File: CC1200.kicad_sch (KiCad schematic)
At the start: 55 parts, among them U3 CC1200, U4 MCP6001-OT, U8 MCP41010, X1 40MHz

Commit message: Revert "Stephen"
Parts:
- removed AE1: Antenna_Shield, Connector_Coaxial:SMA_BAT_Wireless_BWSMA-KWE-Z001, symbol Device:Antenna_Shield
- removed C14: DNM, Capacitor_SMD:C_0402_1005Metric, symbol Device:C
- removed C38, C39, C46: 0.1uF, Capacitor_SMD:C_0402_1005Metric, symbol Device:C
- removed C43, C44, C45: 100pF, Capacitor_SMD:C_0402_1005Metric, symbol Device:C
- removed C47: 10nF, Capacitor_SMD:C_0402_1005Metric, symbol Device:C
- removed JP1: SolderJumper_2_Open, Jumper:SolderJumper-2_P1.3mm_Open_RoundedPad1.0x1.5mm, symbol Jumper:SolderJumper_2_Open
- removed JP2: SolderJumper_2_Bridged, Jumper:SolderJumper-2_P1.3mm_Bridged_RoundedPad1.0x1.5mm, symbol Jumper:SolderJumper_2_Bridged
- removed L8: 22nH, Inductor_SMD:L_0402_1005Metric, symbol pspice:INDUCTOR
- removed R14: 1000, Resistor_SMD:R_0402_1005Metric, symbol Device:R_US
- removed R16: 1k, Resistor_SMD:R_0402_1005Metric, symbol Device:R_Small_US
- removed R2: 100, Resistor_SMD:R_0402_1005Metric, symbol Device:R_US
- removed RFAMP1: RA07H4047M-101, RA07H4047M:RA07H4047M101_HORIZ, symbol RA07H4047M-101:RA07H4047M-101
- removed RFSWITCH2: 4259-63, PE4259-63:SOT65P210X110-6N, symbol 4259-63:4259-63
- removed TH1: PT100, Resistor_SMD:R_0603_1608Metric, symbol Sensor_Temperature:PT100
- removed U4: MCP6001-OT, Package_TO_SOT_SMD:SOT-23-5, symbol Amplifier_Operational:MCP6001-OT
- removed U8: MCP41010, MCP41010:SOIC127P599X175-8N, symbol Potentiometer_Digital:MCP41010
- added A: AMP, symbol Device:R
- added RV1: R_Potentiometer, symbol Device:R_Potentiometer
- added SW1, SW2: SW_SPDT, symbol Switch:SW_SPDT
- C15, C17, C18, C19, C23, C24, C25, C28, C29: LCSC C272875 -> (none); LCSC Part (none) -> C508865
- C16: LCSC C16772 -> (none); LCSC Part (none) -> C16772
- C20, C22: LCSC C15195 -> (none); LCSC Part (none) -> C15195
- C21: value 1.5nF -> 1.8nF; LCSC C107022 -> (none); LCSC Part (none) -> C162192
- C26: LCSC C1572 -> (none); LCSC Part (none) -> C335543
- C27: LCSC C126492 -> (none); LCSC Part (none) -> C126492
- C30: LCSC C106223 -> (none); LCSC Part (none) -> C86288
- C31, C36: value 20pF -> 10pF; LCSC C1554 -> (none); LCSC Part (none) -> C32949
- C32, C33, C35: LCSC C60220 -> (none); LCSC Part (none) -> C281761
- C34: LCSC C325452 -> (none); LCSC Part (none) -> C159806
- C37: LCSC C41744 -> (none); LCSC Part (none) -> C325456
- L1, L2: footprint Inductor_SMD:L_0402_1005Metric -> Capacitor_SMD:C_0402_1005Metric; LCSC C167482 -> (none); LCSC Part (none) -> C167484
- L3: footprint Inductor_SMD:L_0402_1005Metric -> Capacitor_SMD:C_0402_1005Metric
- L4: footprint Inductor_SMD:L_0402_1005Metric -> Capacitor_SMD:C_0402_1005Metric; LCSC C12669 -> (none); LCSC Part (none) -> C12669
- L5, L6: footprint Inductor_SMD:L_0402_1005Metric -> Capacitor_SMD:C_0402_1005Metric; LCSC C94079 -> (none); LCSC Part (none) -> C27143
- L7: value 43nH -> 22nH; footprint Inductor_SMD:L_0402_1005Metric -> Capacitor_SMD:C_0402_1005Metric; LCSC C167478 -> (none); LCSC Part (none) -> C12670
- R13: footprint Resistor_SMD:R_0402_1005Metric -> Capacitor_SMD:C_0402_1005Metric; LCSC C138289 -> (none); LCSC Part (none) -> C138289
- R8: footprint Resistor_SMD:R_0402_1005Metric -> Capacitor_SMD:C_0402_1005Metric; LCSC C25796 -> (none); LCSC Part (none) -> C25796
- R9: value 18 -> 18k; footprint Resistor_SMD:R_0402_1005Metric -> Capacitor_SMD:C_0402_1005Metric; LCSC C2929991 -> (none); LCSC Part (none) -> C25084
- U3: LCSC C122881 -> (none); LCSC Part (none) -> C122881
- X1: LCSC C9010 -> (none); LCSC Part (none) -> C9010
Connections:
- net GND: now also C35.2
- net RX: no longer C33.1, L3.2
- net at L7.1: now also C34.1, C35.1, L5.2; no longer C37.1
- net at R13.1: now also C37.1, L7.2
- new net: A.1, SW1.1 (A)
- new net: SW1.3 (C), SW2.3 (C)
- new net: A.2, SW2.1 (A)
- new net: C33.1, L3.2, L6.1
- new net ANT: SW2.2 (B)
- new net CC1200: SW1.2 (B)
- now unconnected: U3.18 (TRX_SW)
- no-connect marks 1 -> 2
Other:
- note added: "TODO: Verify TX vs RX topology + matching Switch from seperate TX/RX to OG coupled RX / TX (do a bit of research first to which is better) Add amp bypass switch Add amp Add DPOT + OPAMP Buffer for Gate Voltage Add RTD (temp sensor)"
- note removed: "* Data sheet uses 1k pull-ups, can change back to 10k if needed."
- note removed: "*In single-pin control configuration, since we want no amplification by default, CTRL pin 4 is pulled high by default, allowing signal path of RFC -> RF1"
- note removed: "*RTD100 0603 is low on stock (~250), may need to replace with something else if it goes out of stock, such as a more complicated sensor or ic. Also may want to swap VD orientation."
- note removed: "1.8 nF -> 1.5 nF (changed from RS)"
- note removed: "Changed C31 and C36 to 20 pF from 10 pF each based on C9010 crystal needing 15 pF load capacitance overall, and using equation C1=C2=2*(C_L-C_stray), approximating C_stray as 5 pF."
- note removed: "TEMPERATURE SENSING"
- note removed: "keep dpot and op amp close to stm32, far from antenna"
- moved on the sheet: C37, L4, L5, L6, L7, R13

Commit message: checked matching network on CC1200 schematic
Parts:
- added C14: DNM, Capacitor_SMD:C_0402_1005Metric, symbol Device:C
- added L8: 22nH, Inductor_SMD:L_0402_1005Metric, symbol pspice:INDUCTOR
- C15, C17, C18, C19, C23, C24, C25, C28, C29: LCSC (none) -> C272875; LCSC Part C508865 -> (none)
- C16: LCSC (none) -> C16772; LCSC Part C16772 -> (none)
- C20, C22: LCSC (none) -> C15195; LCSC Part C15195 -> (none)
- C21: value 1.8nF -> 1.5nF; LCSC (none) -> C107022; LCSC Part C162192 -> (none)
- C26: LCSC (none) -> C1572; LCSC Part C335543 -> (none)
- C27: LCSC (none) -> C126492; LCSC Part C126492 -> (none)
- C30: LCSC (none) -> C106223; LCSC Part C86288 -> (none)
- C31, C36: value 10pF -> 20pF; LCSC (none) -> C1554; LCSC Part C32949 -> (none)
- C32, C33, C35: LCSC (none) -> C60220; LCSC Part C281761 -> (none)
- C34: LCSC (none) -> C325452; LCSC Part C159806 -> (none)
- C37: LCSC (none) -> C41744; LCSC Part C325456 -> (none)
- L1, L2: footprint Capacitor_SMD:C_0402_1005Metric -> Inductor_SMD:L_0402_1005Metric; LCSC (none) -> C167482; LCSC Part C167484 -> (none)
- L3: footprint Capacitor_SMD:C_0402_1005Metric -> Inductor_SMD:L_0402_1005Metric
- L4: footprint Capacitor_SMD:C_0402_1005Metric -> Inductor_SMD:L_0402_1005Metric; LCSC (none) -> C12669; LCSC Part C12669 -> (none)
- L5, L6: footprint Capacitor_SMD:C_0402_1005Metric -> Inductor_SMD:L_0402_1005Metric; LCSC (none) -> C94079; LCSC Part C27143 -> (none)
- L7: value 22nH -> 43nH; footprint Capacitor_SMD:C_0402_1005Metric -> Inductor_SMD:L_0402_1005Metric; LCSC (none) -> C167478; LCSC Part C12670 -> (none)
- R8: footprint Capacitor_SMD:C_0402_1005Metric -> Resistor_SMD:R_0402_1005Metric; LCSC (none) -> C25796; LCSC Part C25796 -> (none)
- R9: value 18k -> 18; footprint Capacitor_SMD:C_0402_1005Metric -> Resistor_SMD:R_0402_1005Metric; LCSC (none) -> C2929991; LCSC Part C25084 -> (none)
- X1: LCSC (none) -> C9010; LCSC Part C9010 -> (none)
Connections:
- net at C37.1, L7.2: now also C14.1, L8.1; no longer R13.1
- new net: C14.2, L8.2, R13.1
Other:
- note added: "*Check with Ethan that we are not using external oscillator, if so this should be fine just tied to ground, but reference schematic looks different."
- note added: "*Don't know if this capacitor should connect here, depends on if we are using TRX_SW pin on CC1200 and if we are or aren't coupling the LNA and PA pins."
- note added: "1.8 nF -> 1.5 nF (changed from RS)"
- note added: "Changed C31 and C36 to 20 pF from 10 pF each based on C9010 crystal needing 15 pF load capacitance overall, and using equation C1=C2=2*(C_L-C_stray), approximating C_stray as 5 pF."
- note added: "TODO: Verify TX vs RX topology + matching (DONE) Switch from seperate TX/RX to OG coupled RX / TX (do a bit of research first to which is better) Add amp bypass switch Add amp Add DPOT + OPAMP Buffer for Gate Voltage Add RTD (temp sensor)"
- note removed: "TODO: Verify TX vs RX topology + matching Switch from seperate TX/RX to OG coupled RX / TX (do a bit of research first to which is better) Add amp bypass switch Add amp Add DPOT + OPAMP Buffer for Gate Voltage Add RTD (temp sensor)"
- moved on the sheet: C37, L6, R13

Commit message: completed most of radio schematic
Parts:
- removed A: AMP, symbol Device:R
- removed RV1: R_Potentiometer, symbol Device:R_Potentiometer
- removed SW1, SW2: SW_SPDT, symbol Switch:SW_SPDT
- added C38, C39, C40: 100pF, Capacitor_SMD:C_0402_1005Metric, symbol Device:C
- added C41, C42: 33pF, Capacitor_SMD:C_0402_1005Metric, symbol Device:C
- added J6: SMA_CONNECTOR, Connector_Coaxial:SMA_Amphenol_901-143_Horizontal, symbol SMA_CONNECTOR:SMA_CONNECTOR
- added R14, R2: 4.7k, Resistor_SMD:R_0402_1005Metric, symbol Device:R_Small_US
- added RFAMP: ~, symbol RA07H4047M:RA07H4047M_RF_MOSFET_AMPLIFIER
- added RFSWITCH: SKY13351-378LF, SKY13351-378LF:QFN6-LF, symbol SKY13351-378LF:SKY13351-378LF
- added TH1: Thermistor_US, symbol Device:Thermistor_US
- added U4: MCP6001-OT, Package_TO_SOT_SMD:SOT-23-5, symbol Amplifier_Operational:MCP6001-OT
- R13: footprint Capacitor_SMD:C_0402_1005Metric -> Resistor_SMD:R_0402_1005Metric; LCSC (none) -> C138289; LCSC Part C138289 -> (none)
- U3: LCSC (none) -> C122881; LCSC Part C122881 -> (none)
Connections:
- net +3.3V: now also R2.2
- net GND: now also C41.2, C42.1, J6.G1, J6.G2, J6.G3, J6.G4, R14.1, RFAMP.5 (GND), RFSWITCH.2; no longer C35.2
- net RX: now also C33.1, L3.2
- net TX: now also C38.1
- net at U3.18 (TRX_SW): now also C35.1, L6.1
- net at C34.1, L5.2, L7.1: now also C35.2; no longer C35.1
- new net: C39.1, RFSWITCH.3 (OUTPUT2)
- new net: C39.2, J6.1, RFAMP.4 (RFOUT)
- new net: C38.2, RFSWITCH.5 (INPUT)
- new net: C40.1, RFSWITCH.1 (OUTPUT1)
- new net: C40.2, RFAMP.1 (RFIN)
- new net: RFAMP.2 (VGG), U4.1, U4.4 (-)
- new net +BATT: RFAMP.3 (VDD)
- new net VCTL1: C42.2, R2.1, RFSWITCH.6
- new net VCTL2: C41.1, R14.2, RFSWITCH.4
- no-connect marks 2 -> 1
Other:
- note added: "*C38, C39, and C40 are 100 pF DC blocking capacitors for the RF inputs and outputs per the datasheet."
- note added: "*C41 and C42 are 33 pF bypass capacitors per the datasheet."
- note added: "*Pulling VCTL1 pin to high and VCTL2 pin to low with pull-ups/pull-downs assuming we want to amplify the transmitted signal by default, but can change if needed."
- note added: "*Weird overlap on the text is just because the bottom pin is representing all the outside pins of the SMA connector that are connected to ground, while the top pin is just the signal input into the connector."
- note added: "TODO AFTER LUNCH: 1. Wire together RF switch with amplifier and antenna, also connecting control pin to the stm32 (DONE!) 2. Configure V_GG for RFAMP, using dpot/temp resisitor voltage divider, op-amp voltage follower, and RC LPF before ADC 3. Make footprint for RF amp (can do after pushing and sending Ethan schematic to look over though)"
- note added: "TODO: Verify TX vs RX topology + matching (DONE) Switch from seperate TX/RX to OG coupled RX / TX (do a bit of research first to which is better) (DONE) Add amp bypass switch (DONE) Add amp (symbol DONE, footprint in progress) Add DPOT + OPAMP Buffer for Gate Voltage Add RTD (temp sensor)"
- note removed: "*Don't know if this capacitor should connect here, depends on if we are using TRX_SW pin on CC1200 and if we are or aren't coupling the LNA and PA pins."
- note removed: "TODO: Verify TX vs RX topology + matching (DONE) Switch from seperate TX/RX to OG coupled RX / TX (do a bit of research first to which is better) Add amp bypass switch Add amp Add DPOT + OPAMP Buffer for Gate Voltage Add RTD (temp sensor)"
- moved on the sheet: C14, C37, L4, L5, L6, L7, L8, R13

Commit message: changed rf switch, updated rf amp footprint and updated schematic
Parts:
- removed C38, C39, C40: 100pF, Capacitor_SMD:C_0402_1005Metric, symbol Device:C
- removed C41, C42: 33pF, Capacitor_SMD:C_0402_1005Metric, symbol Device:C
- removed J6: SMA_CONNECTOR, Connector_Coaxial:SMA_Amphenol_901-143_Horizontal, symbol SMA_CONNECTOR:SMA_CONNECTOR
- removed R14, R2: 4.7k, Resistor_SMD:R_0402_1005Metric, symbol Device:R_Small_US
- removed RFAMP: ~, symbol RA07H4047M:RA07H4047M_RF_MOSFET_AMPLIFIER
- removed RFSWITCH: SKY13351-378LF, SKY13351-378LF:QFN6-LF, symbol SKY13351-378LF:SKY13351-378LF
- added AE1: Antenna_Shield, symbol Device:Antenna_Shield
- added C43, C44, C45: 100pF, Capacitor_SMD:C_0402_1005Metric, symbol Device:C
- added C46: 0.1uF, Capacitor_SMD:C_0402_1005Metric, symbol Device:C
- added C47: 10nF, Capacitor_SMD:C_0402_1005Metric, symbol Device:C
- added JP1: SolderJumper_2_Open, symbol Jumper:SolderJumper_2_Open
- added JP2: SolderJumper_2_Bridged, symbol Jumper:SolderJumper_2_Bridged
- added R16: 1k, Resistor_SMD:R_0402_1005Metric, symbol Device:R_Small_US
- added R2: 100, Resistor_SMD:R_0402_1005Metric, symbol Device:R_US
- added RFAMP1: RA07H4047M-101, RA07H4047M:RA07H4047M101, symbol RA07H4047M-101:RA07H4047M-101
- added RFSWITCH2: 4259-63, PE4259-63:SOT65P210X110-6N, symbol 4259-63:4259-63
- added U5: MCP41010, symbol Potentiometer_Digital:MCP41010
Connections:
- net +3.3V: now also TH1.1, U4.5 (V+), C46.2, R16.2, RFSWITCH2.6 (~{CTRL_OR_VDD}), U5.5 (PA0), U5.8 (VDD)
- net +BATT: now also RFAMP1.3 (DRAIN_VOLTAGE_(VDD))
- net GND: now also U4.2 (V-), AE1.2 (Shield), C46.1, C47.1, R2.2, RFAMP1.5 (GND), RFSWITCH2.2 (GND), U5.4 (VSS), U5.7 (PB0)
- net TX: now also C43.1
- net at U4.1, U4.4 (-): now also RFAMP1.2 (GATE_VOLTAGE_(VGG))
- net at U4.3 (+): now also JP1.1 (A), JP2.2 (B)
- net THERMISTORADC: now reaches TH1.2
- net THERMISTORADC: now also R2.1
- new net: JP2.1 (A), U5.6 (PW0)
- new net: C45.1, RFSWITCH2.1 (RF1)
- new net: AE1.1 (A), C45.2, RFAMP1.4 (RF_OUTPUT_(POUT))
- new net: C44.1, RFSWITCH2.3 (RF2)
- new net: C44.2, RFAMP1.1 (RF_INPUT_(PIN))
- new net: C43.2, RFSWITCH2.5 (RFC)
- new net AMP_ON: JP1.2 (B)
- new net VCTL: C47.2, R16.1, RFSWITCH2.4 (CTRL)
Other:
- note added: "* Data sheet uses 1k pull-ups, can change back to 10k if needed."
- note added: "*In single-pin control configuration, since we want no amplification by default, CTRL pin 4 is pulled high by default, allowing signal path of RFC -> RF1"
- note added: "*Need a digital temp sensor here right? In place of the thermistor"
- note added: "*Will connect later, haven't gotten around to it yet"
- note added: "keep dpot and op amp close to stm32, far from antenna"
- note added: "put LPF before adc."
- note removed: "*C38, C39, and C40 are 100 pF DC blocking capacitors for the RF inputs and outputs per the datasheet."
- note removed: "*C41 and C42 are 33 pF bypass capacitors per the datasheet."
- note removed: "*Check with Ethan that we are not using external oscillator, if so this should be fine just tied to ground, but reference schematic looks different."
- note removed: "*Pulling VCTL1 pin to high and VCTL2 pin to low with pull-ups/pull-downs assuming we want to amplify the transmitted signal by default, but can change if needed."
- note removed: "*Weird overlap on the text is just because the bottom pin is representing all the outside pins of the SMA connector that are connected to ground, while the top pin is just the signal input into the connector."
- note removed: "TODO AFTER LUNCH: 1. Wire together RF switch with amplifier and antenna, also connecting control pin to the stm32 (DONE!) 2. Configure V_GG for RFAMP, using dpot/temp resisitor voltage divider, op-amp voltage follower, and RC LPF before ADC 3. Make footprint for RF amp (can do after pushing and sending Ethan schematic to look over though)"
- note removed: "TODO: Verify TX vs RX topology + matching (DONE) Switch from seperate TX/RX to OG coupled RX / TX (do a bit of research first to which is better) (DONE) Add amp bypass switch (DONE) Add amp (symbol DONE, footprint in progress) Add DPOT + OPAMP Buffer for Gate Voltage Add RTD (temp sensor)"

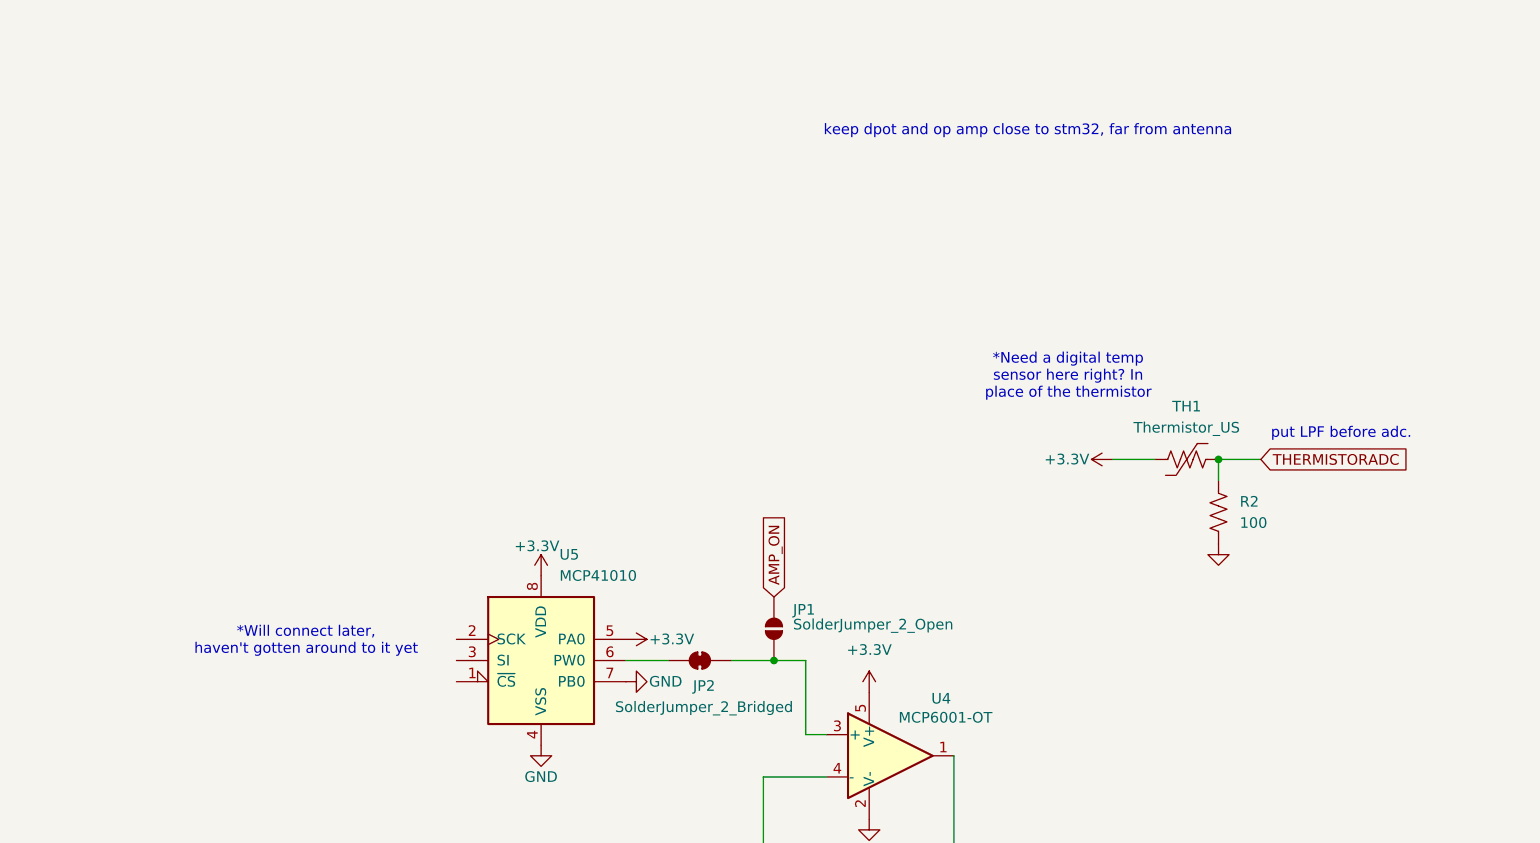
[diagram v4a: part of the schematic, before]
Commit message: fixed temp sensor and updated digpot stm32 connections
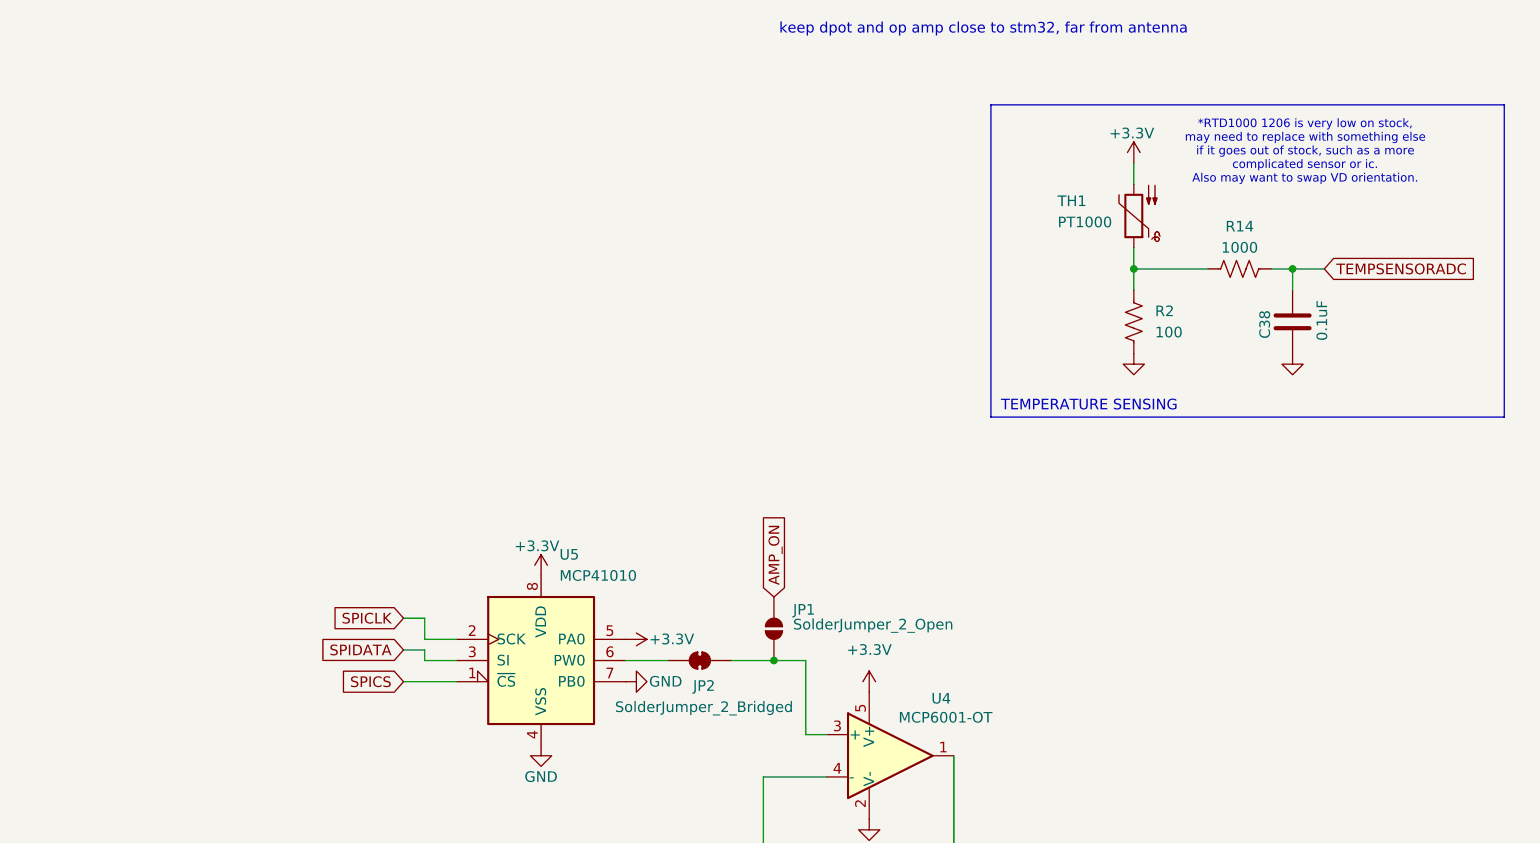
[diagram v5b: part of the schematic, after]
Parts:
- removed TH1: Thermistor_US, symbol Device:Thermistor_US
- added C38: 0.1uF, Capacitor_SMD:C_0402_1005Metric, symbol Device:C
- added R14: 1000, Resistor_SMD:R_0402_1005Metric, symbol Device:R_US
- added TH1: PT1000, Resistor_SMD:R_1206_3216Metric, symbol Sensor_Temperature:PT1000
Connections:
- net +3.3V: now also TH1.2
- net GND: now also C38.2
- net SPICS: now reaches U5.1 (~{CS})
- net SPICLK: now reaches U5.2 (SCK)
- net SPIDATA: now reaches U5.3 (SI)
- net THERMISTORADC: no longer names the net of R2.1
- net THERMISTORADC: now also R14.1, TH1.1
- new net TEMPSENSORADC: C38.1, R14.2
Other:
- note added: "*RTD1000 1206 is very low on stock, may need to replace with something else if it goes out of stock, such as a more complicated sensor or ic. Also may want to swap VD orientation."
- note added: "TEMPERATURE SENSING"
- note removed: "*Need a digital temp sensor here right? In place of the thermistor"
- note removed: "*Will connect later, haven't gotten around to it yet"
- note removed: "put LPF before adc."
- moved on the sheet: R2
